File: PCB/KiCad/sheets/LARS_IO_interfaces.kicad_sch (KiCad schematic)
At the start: 52 parts, among them J10 I2C1, J11 I2C1, J12 TIM1, J13 TIM2, J14 I2C2, J15 I2C2, J16 I2C2, J17 I2C2, J18 3.3V Out, J19 5V Out, J20 UART1, J21 UART2, J22 UART3, J23 Servo 1, J24 Servo 2, J25 GPIO, J26 Analog 1, J27 Analog 2, J4 CAN1, J5 CAN1, J6 SPI1, J7 SPI1, J8 I2C1, J9 I2C1

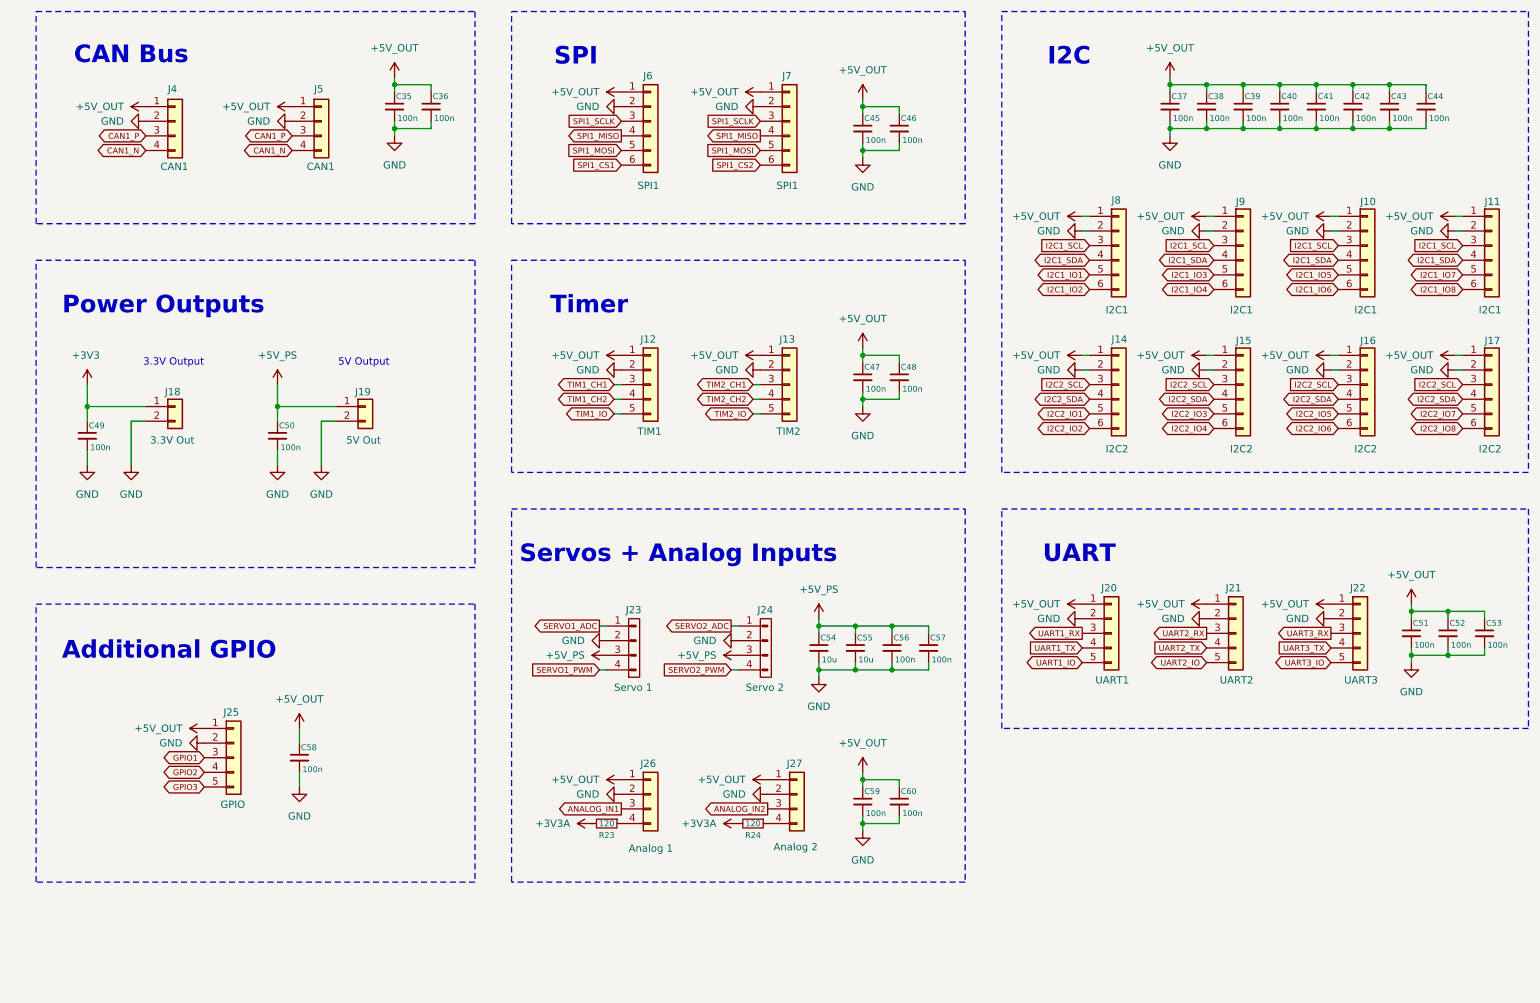
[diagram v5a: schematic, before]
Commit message: PCB: update resistor values and embed font
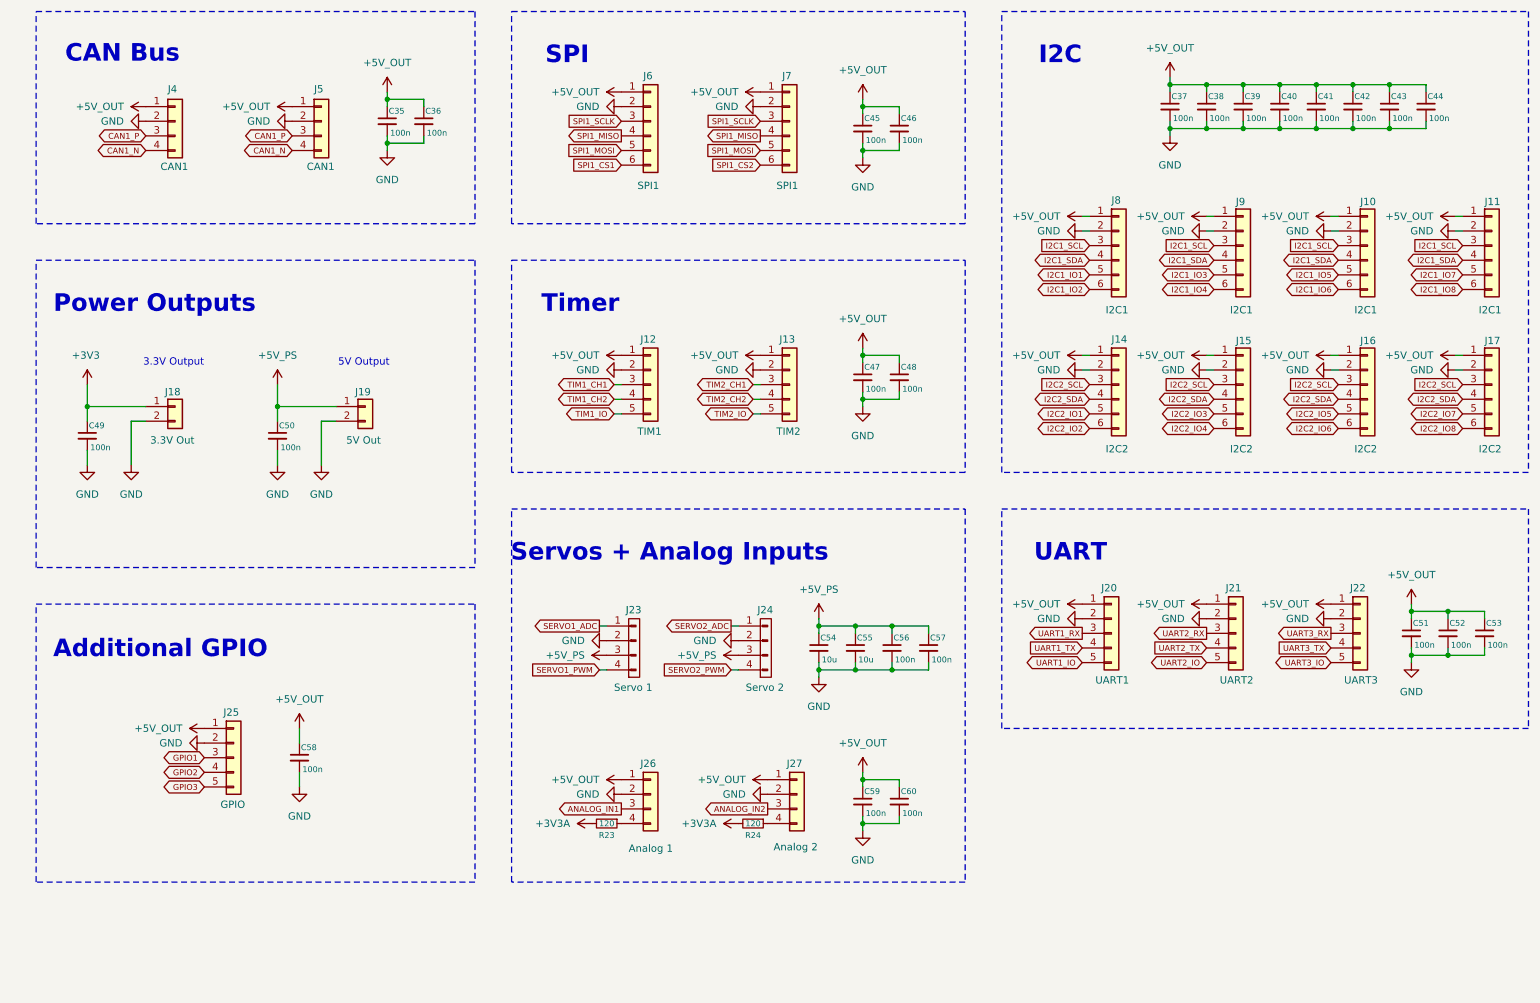
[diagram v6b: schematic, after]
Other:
- moved on the sheet: C35, C36

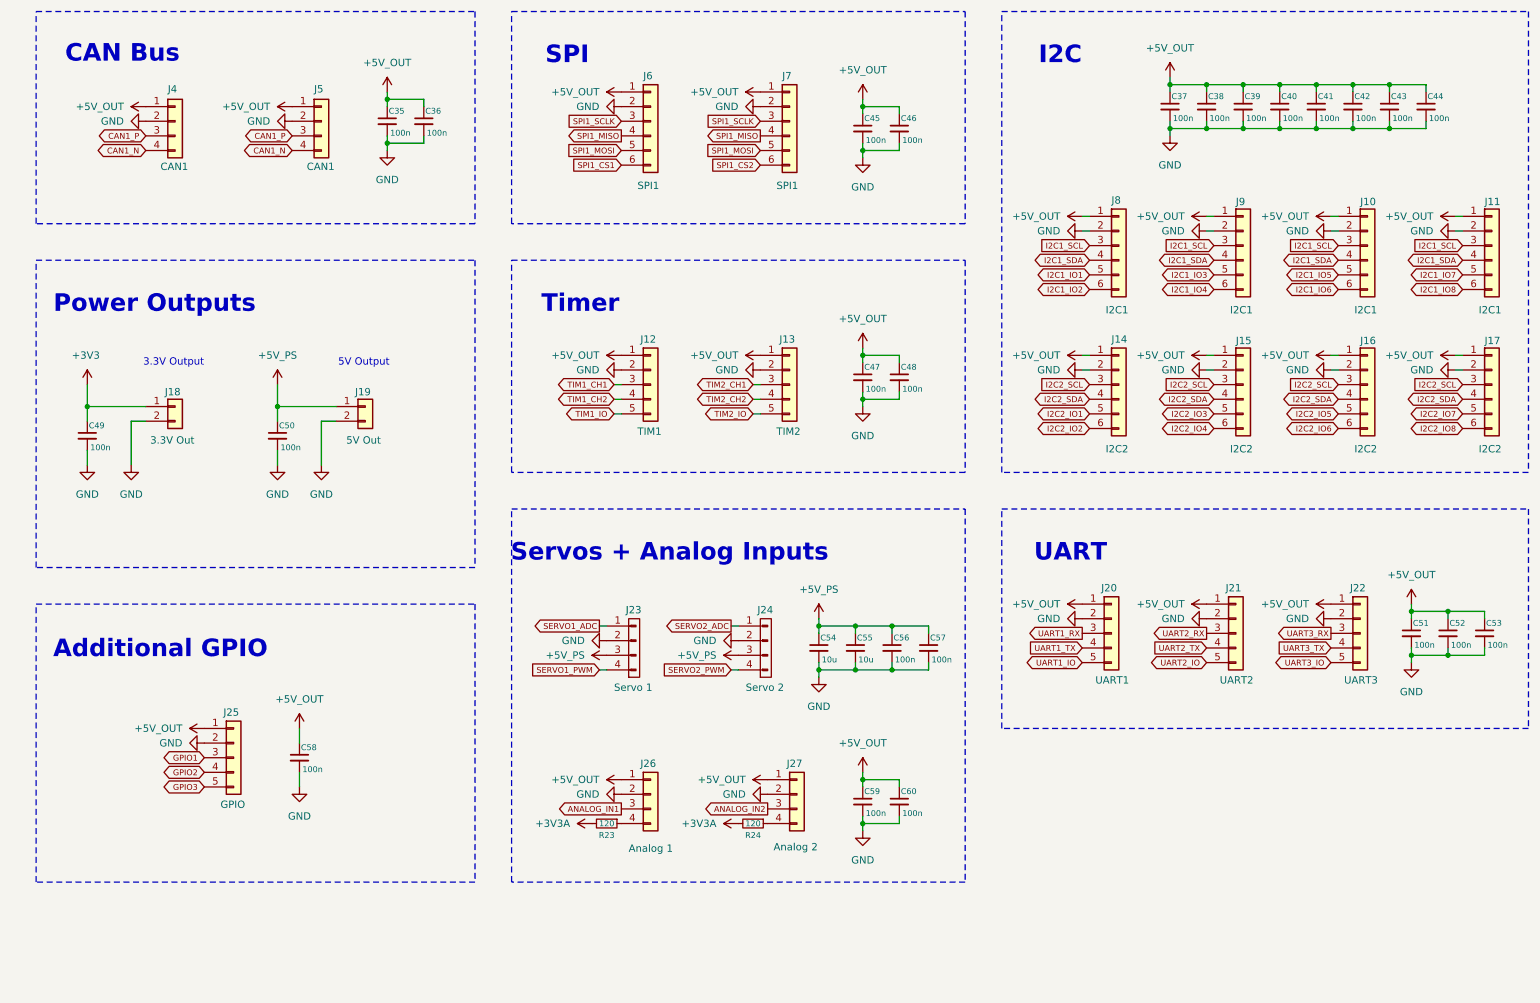
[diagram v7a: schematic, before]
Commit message: PCB: add XOR gate for RC Receiver
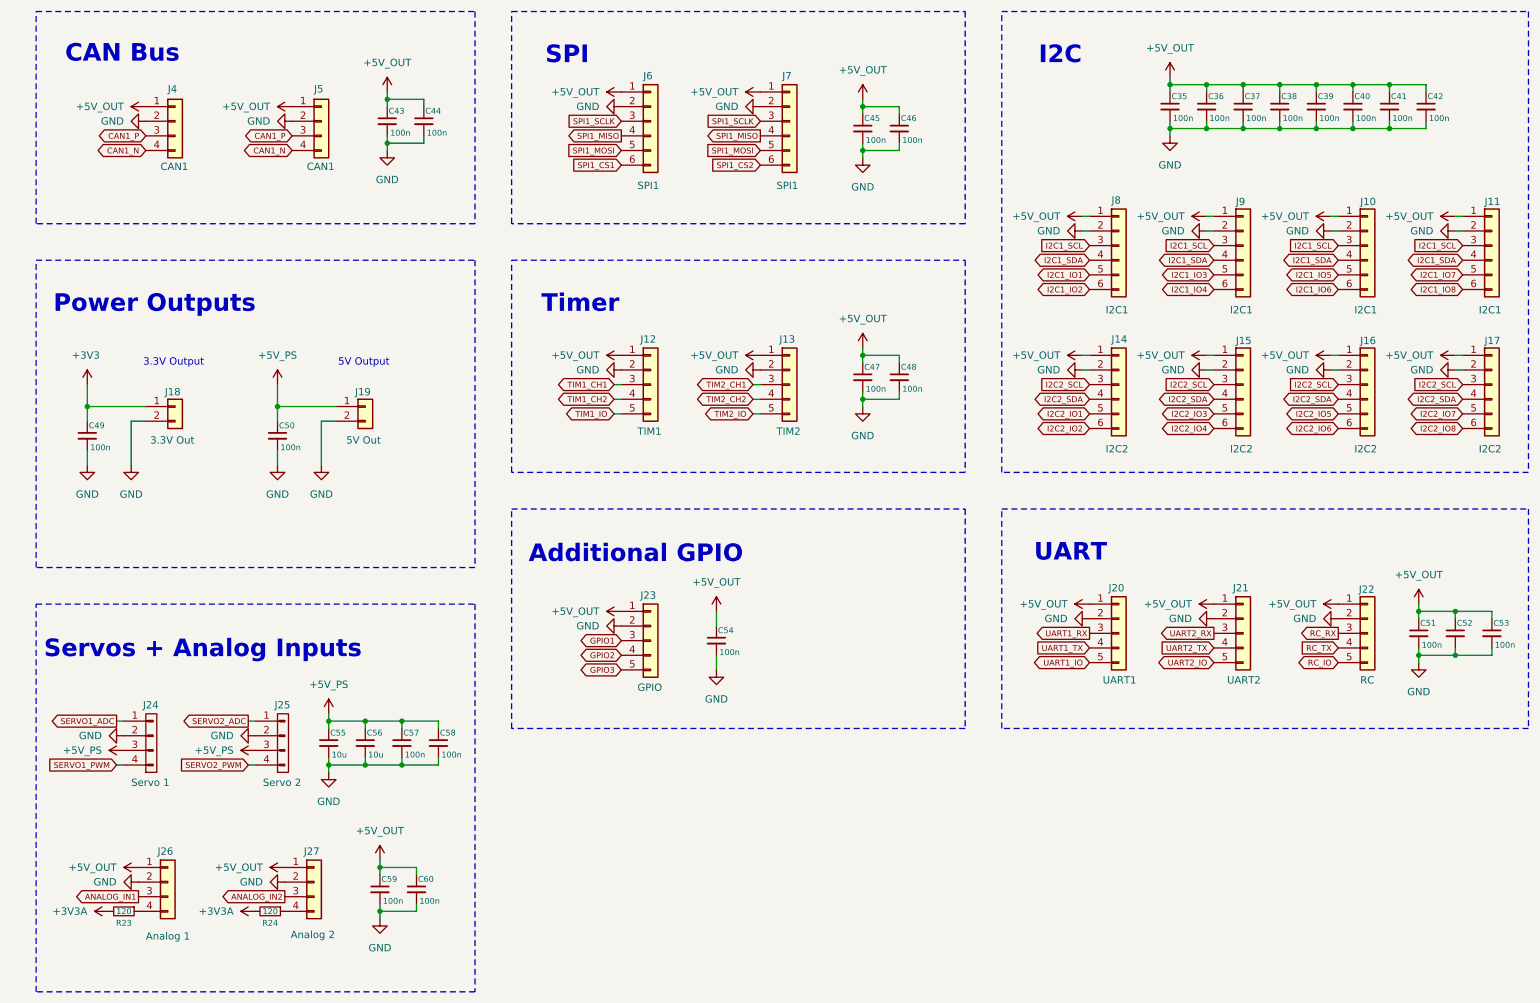
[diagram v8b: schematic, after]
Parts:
- J22: value UART3 -> RC
- renumbered C37 to C35, C38 to C36, C39 to C37, C40 to C38, C41 to C39, C42 to C40, C43 to C41, C44 to C42, C35 to C43, C36 to C44, C58 to C54, C54 to C55, C55 to C56, C56 to C57, C57 to C58, J25 to J23, J23 to J24, J24 to J25
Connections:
- net UART3_IO renamed RC_IO
- net UART3_RX renamed RC_RX
- net UART3_TX renamed RC_TX
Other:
- moved on the sheet: C51, C52, C53, C54, C55, C56, C57, C58, C59, C60, J20, J21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
